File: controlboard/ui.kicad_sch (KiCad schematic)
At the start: 0 parts

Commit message: more progress on controlboard pcb
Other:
- note added: "5V 200mA"
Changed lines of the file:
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@@
+		)
+	)
+	(text "5V 200mA"
+		(exclude_from_sim no)
+		(at 48.768 76.962 0)
+		(effects
+			(font
+				(size 1.27 1.27)
+			)
 		)
 	)

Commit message: erc should be good now
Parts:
- added J8: Conn_01x11, symbol Connector_Generic:Conn_01x11
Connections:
- net 3.3V: now also J8.1 (Pin_1)
- net 5V: now also J8.2 (Pin_2)
- net GND: now also J8.3 (Pin_3)
- net LCD_CS: now also J8.10 (Pin_10)
- net LCD_RS: now also J8.5 (Pin_5)
- net LCD_SCK / TP_SCK: now also J8.9 (Pin_9)
- net LCD_SI / TP_SI: now also J8.6 (Pin_6)
- net RST: now also J8.8 (Pin_8)
- net TP_CS: now also J8.11 (Pin_11)
- net TP_IRQ: now also J8.4 (Pin_4)
- net TP_SO: now also J8.7 (Pin_7)
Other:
- note added: "TODO (for karmanyaah only) verify waveshare display pinout once again"
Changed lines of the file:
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@@
 	(generator_version "8.0")
 	(paper "A4")
+	(text "TODO (for karmanyaah only) verify waveshare display pinout once again"
+		(exclude_from_sim no)
+		(at 70.358 14.986 0)
+		(effects
+			(font
+				(size 1.27 1.27)
+			)
+		)
+	)
 	(text "It's a Pi hat, so don't need to worry about connectors\n\nmaking this to keep track of free pins"
 		(exclude_from_sim no)
@@
 	(hierarchical_label "3.3V"
 		(shape input)
-		(at 52.07 19.05 0)
+		(at 46.99 20.32 0)
 		(fields_autoplaced yes)
 		(effects
@@
 	(hierarchical_label "LCD_RS"
 		(shape input)
-		(at 52.07 34.29 0)
+		(at 46.99 30.48 0)
 		(fields_autoplaced yes)
 		(effects
@@
 	(hierarchical_label "LCD_SCK {slash} TP_SCK"
 		(shape input)
-		(at 52.07 49.53 0)
+		(at 46.99 40.64 0)
 		(fields_autoplaced yes)
 		(effects
@@
 	(hierarchical_label "5V"
 		(shape input)
-		(at 52.07 22.86 0)
+		(at 46.99 22.86 0)
 		(fields_autoplaced yes)
 		(effects
@@
 	(hierarchical_label "TP_IRQ"
 		(shape input)
-		(at 52.07 30.48 0)
+		(at 46.99 27.94 0)
 		(fields_autoplaced yes)
 		(effects
@@
 	(hierarchical_label "TP_SO"
 		(shape input)
-		(at 52.07 41.91 0)
+		(at 46.99 35.56 0)
 		(fields_autoplaced yes)
 		(effects
@@
 	(hierarchical_label "RST"
 		(shape input)
-		(at 52.07 45.72 0)
+		(at 46.99 38.1 0)
 		(fields_autoplaced yes)
 		(effects
@@
 	(hierarchical_label "LCD_SI {slash} TP_SI"
 		(shape input)
-		(at 52.07 38.1 0)
+		(at 46.99 33.02 0)
 		(fields_autoplaced yes)
 		(effects
@@
 	(hierarchical_label "TP_CS"
 		(shape input)
-		(at 52.07 57.15 0)
+		(at 46.99 45.72 0)
 		(fields_autoplaced yes)
 		(effects
@@
 	(hierarchical_label "LCD_CS"
 		(shape input)
-		(at 52.07 53.34 0)
+		(at 46.99 43.18 0)
 		(fields_autoplaced yes)
 		(effects
@@
 	(hierarchical_label "GND"
 		(shape input)
-		(at 52.07 26.67 0)
-		(fields_autoplaced yes)
-		(effects
-			(font
-				(size 1.27 1.27)
-			)
-			(justify left)
-		)
-	)
+		(at 46.99 25.4 0)
+		(fields_autoplaced yes)
+		(effects
+			(font
+				(size 1.27 1.27)
+			)
+			(justify left)
+		)
+	)
+	(symbol
+		(lib_id "Connector_Generic:Conn_01x11")
+		(at 41.91 33.02 0)
+		(mirror y)
+		(unit 1)
+		(exclude_from_sim no)
+		(in_bom no)
+		(on_board no)
+		(dnp yes)
+		(fields_autoplaced yes)
+		(property "Reference" "J8"
+			(at 39.37 31.7499 0)
+			(effects
+				(font
+					(size 1.27 1.27)
+				)
+				(justify left)
+			)
+		)
+		(property "Value" "Conn_01x11"
+			(at 39.37 34.2899 0)
+			(effects
+				(font
+					(size 1.27 1.27)
+				)
+				(justify left)
+			)
+		)
+		(property "Footprint" ""
+			(at 41.91 33.02 0)
+			(effects
+				(font
+					(size 1.27 1.27)
+				)
+				(hide yes)
+			)
+		)
+		(property "Datasheet" "~"
+			(at 41.91 33.02 0)
+			(effects
+				(font
+					(size 1.27 1.27)
+				)
+				(hide yes)
+			)
+		)
+		(property "Description" "Generic connector, single row, 01x11, script generated (kicad-library-utils/schlib/autogen/connector/)"
+			(at 41.91 33.02 0)
+			(effects
+				(font
+					(size 1.27 1.27)
+				)
+				(hide yes)
+			)
+		)
+		(pin "2"
+		)
+		(pin "5"
+		)
+		(pin "4"
+		)
+		(pin "6"
+		)
+		(pin "11"
+		)
+		(pin "1"
+		)
+		(pin "9"
+		)
+		(pin "8"
+		)
+		(pin "7"
+		)
+		(pin "3"
+		)
+		(pin "10"
+		)
+		(instances
+			(project "controlboard"
+				(path "/2797250d-6fee-4769-b4dd-0e20ce4f0941/765b86b2-b0cc-4f3c-b57e-87a89e7dcfe3"
+					(reference "J8")
+					(unit 1)
+				)
+			)
+		)
+	)

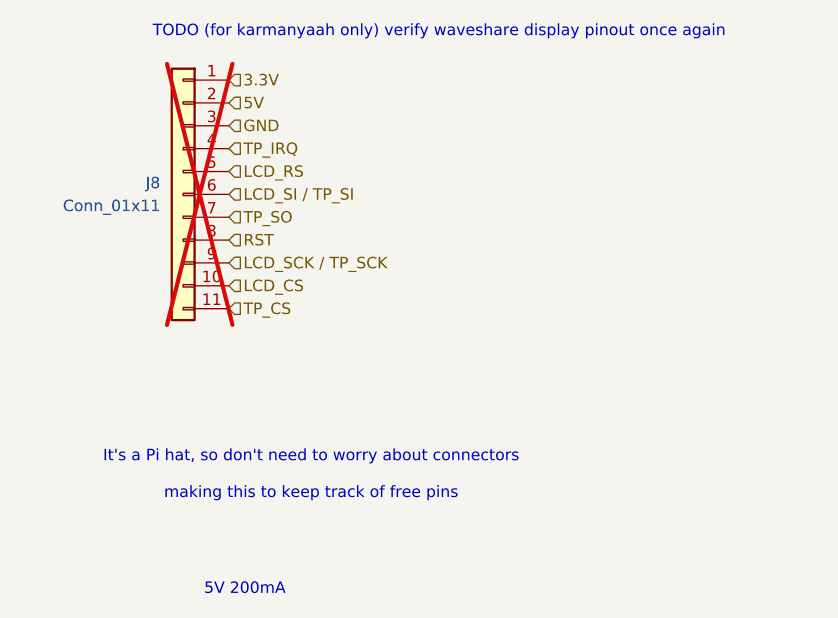
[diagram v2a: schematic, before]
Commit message: controlboard: fix critical mosfet errors
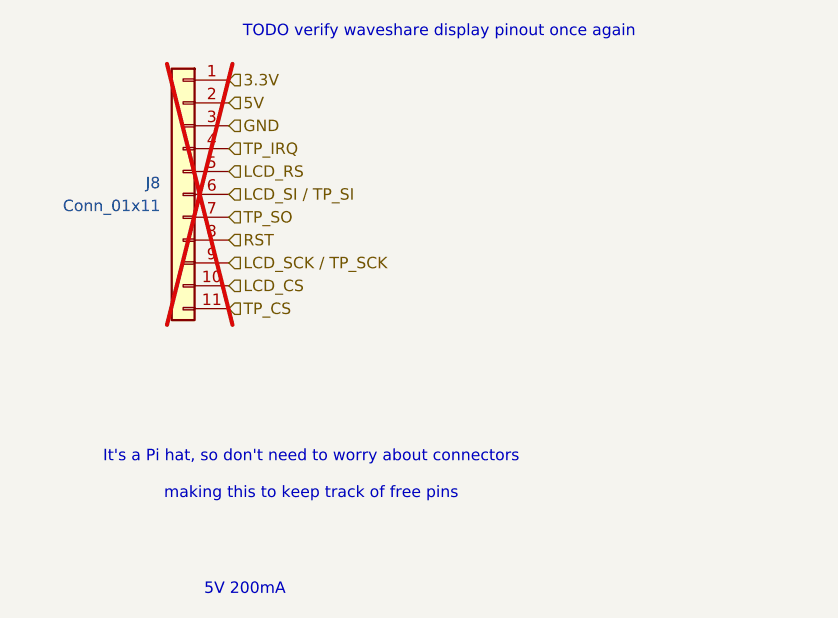
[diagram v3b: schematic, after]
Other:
- note added: "TODO verify waveshare display pinout once again"
- note removed: "TODO (for karmanyaah only) verify waveshare display pinout once again"
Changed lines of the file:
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@@
 	(generator_version "8.0")
 	(paper "A4")
-	(text "TODO (for karmanyaah only) verify waveshare display pinout once again"
+	(text "TODO verify waveshare display pinout once again"
 		(exclude_from_sim no)
 		(at 70.358 14.986 0)
